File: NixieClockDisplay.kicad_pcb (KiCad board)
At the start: 2 copper layers, 160.1 x 160.1 mm, 59 parts, among them J1 CONN_01X08, J2 CONN_01X03, J3 CONN_01X03, U1 TPIC6B595, U2 TPIC6B595, U3 TPIC6B595, U4 TPIC6B595, U5 TPIC6B595, U6 TPIC6B595, U7 WE-FDSM_DC/DC_5V

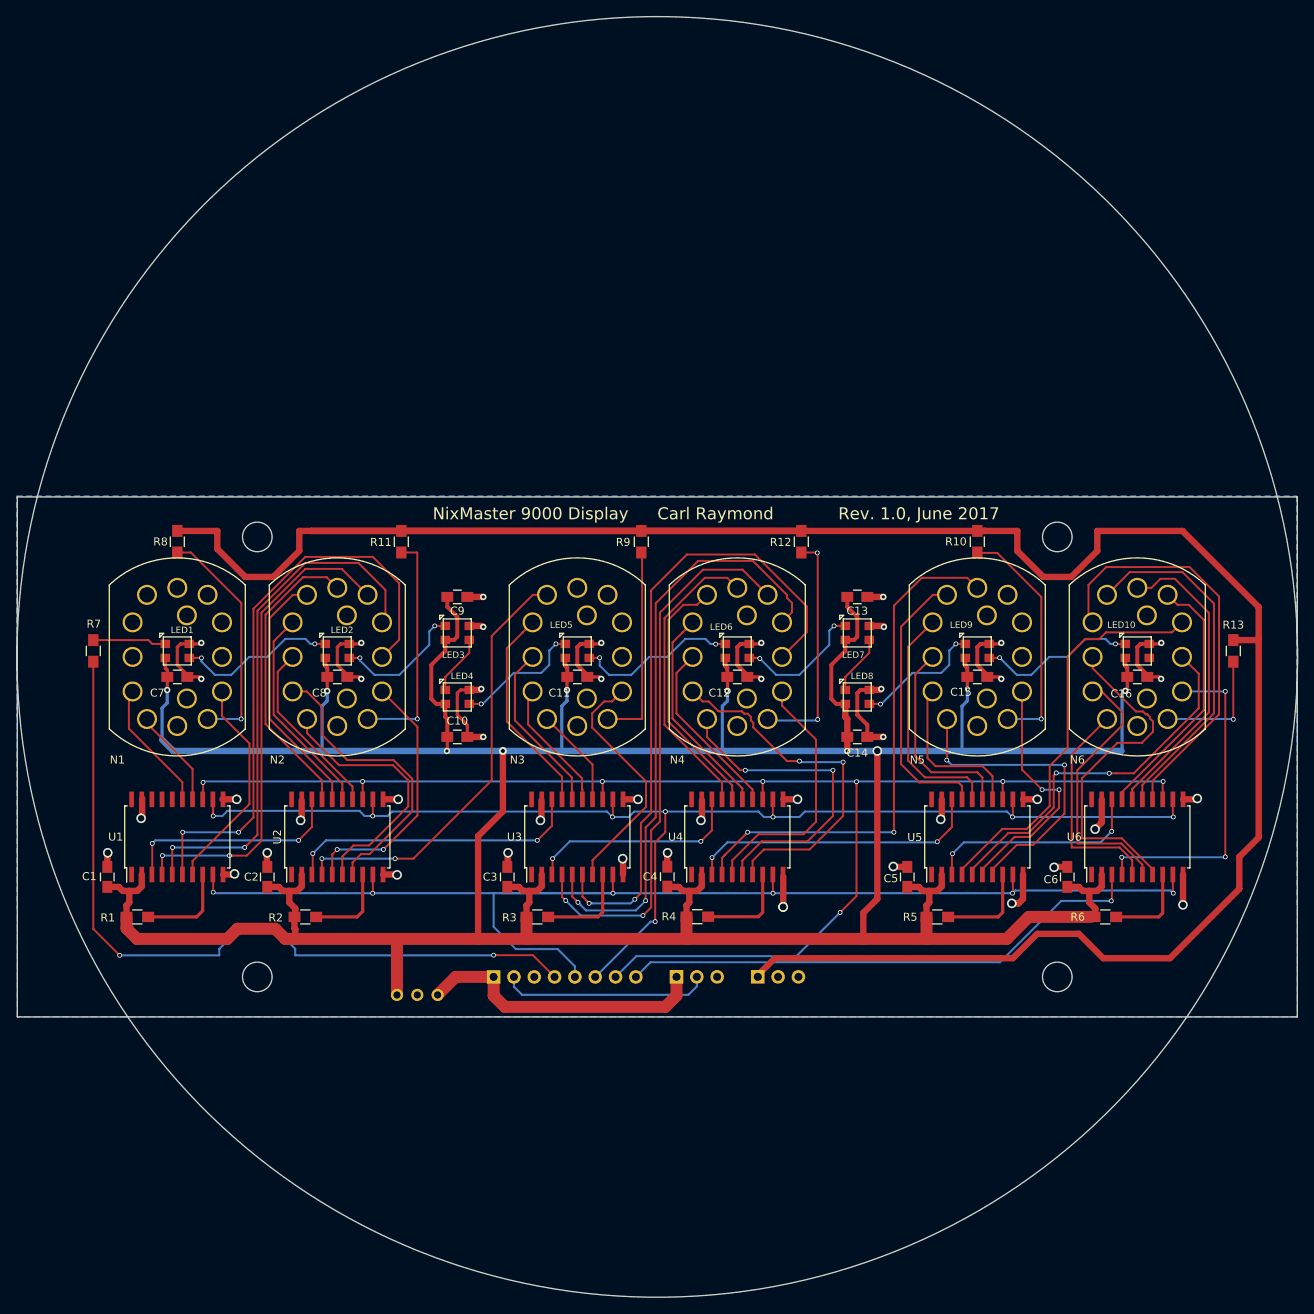
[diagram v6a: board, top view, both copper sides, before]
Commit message: Curved board outline
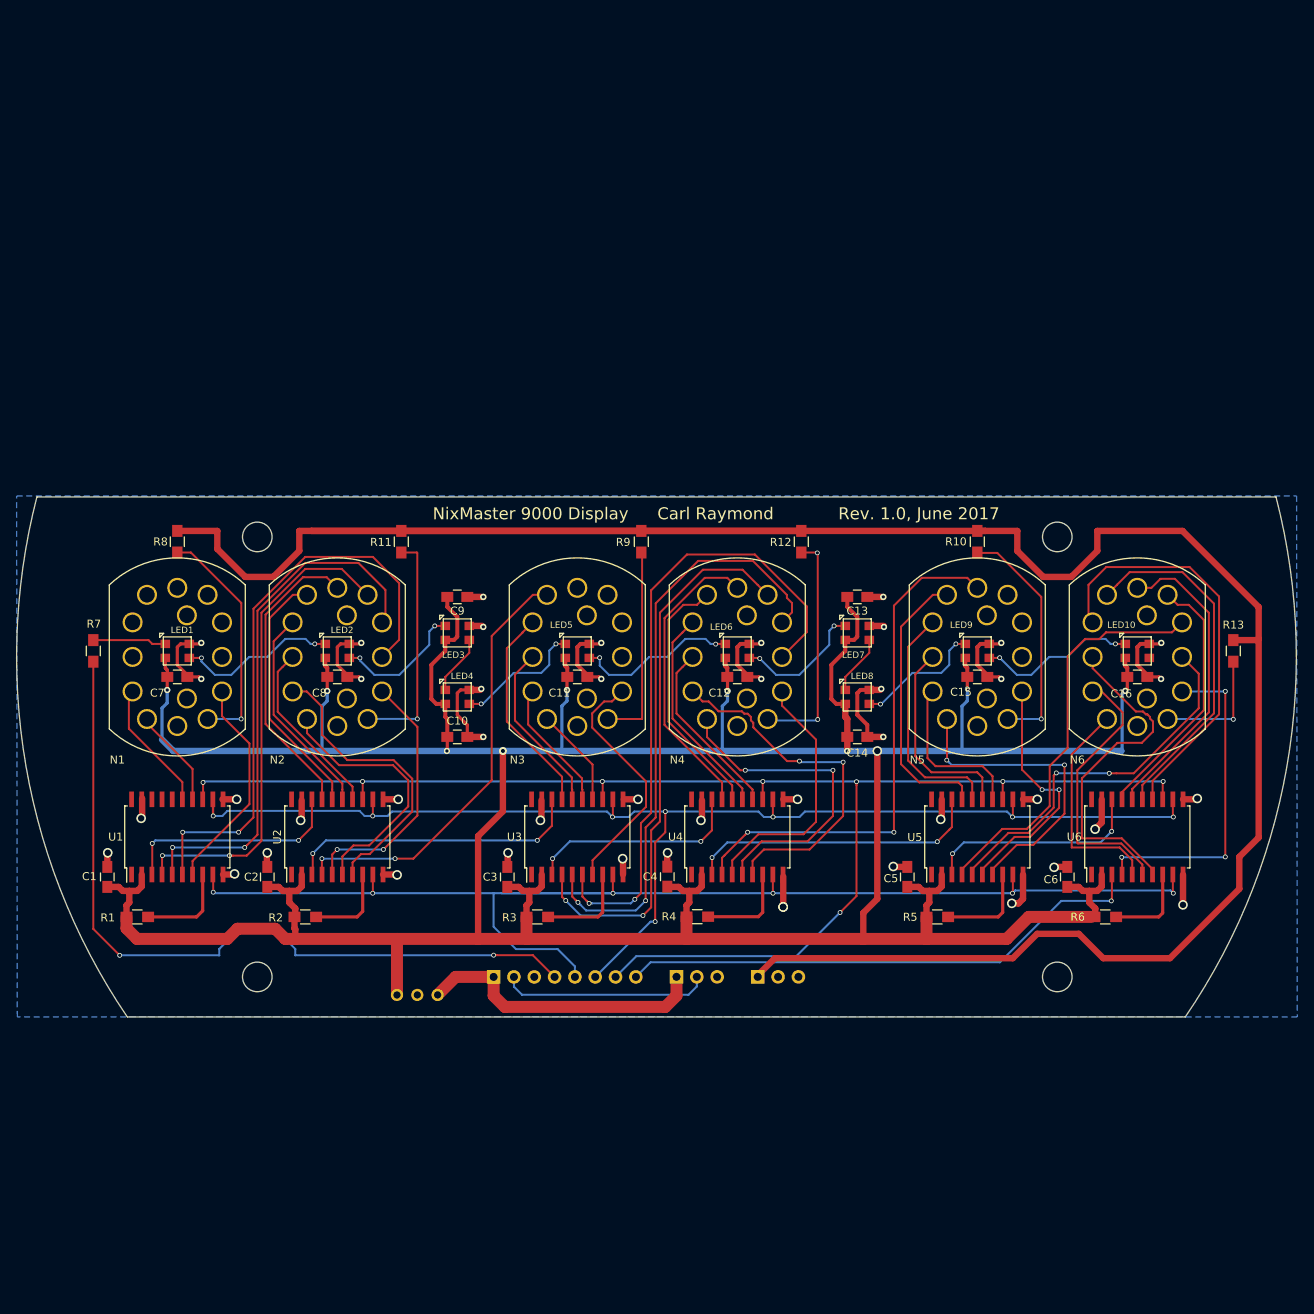
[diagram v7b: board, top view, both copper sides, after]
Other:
- board size 160.1 x 160.1 mm -> 160 x 65 mm
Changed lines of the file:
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@@
   (general
     (links 187)
-    (no_connects 3)
-    (area 69.885946 -20.114054 230.114054 140.350392)
+    (no_connects 0)
+    (area 69.837157 39.906641 229.956163 105.075001)
     (thickness 1.6)
-    (drawings 23)
+    (drawings 22)
     (tracks 1161)
     (zones 0)
@@
   )
   (setup
-    (last_trace_width 0.8)
+    (last_trace_width 0.25)
     (user_trace_width 0.4)
     (user_trace_width 0.5)
@@
     (pad 1 np_thru_hole circle (at 0 0) (size 3.7 3.7) (drill 3.7) (layers *.Cu *.Mask))
   )
-  (gr_circle (center 150 60) (end 230 57.5) (layer Edge.Cuts) (width 0.15))
+  (gr_arc (start 150 60) (end 83.75 105) (angle 48.65) (layer Edge.Cuts) (width 0.15))
+  (gr_arc (start 150 60) (end 216 105) (angle -48.785) (layer Edge.Cuts) (width 0.15))
+  (gr_line (start 216 105) (end 83.75 105) (layer Edge.Cuts) (width 0.15))
+  (gr_line (start 72.45 40) (end 227.33 40) (layer Edge.Cuts) (width 0.15))
   (gr_text "Rev. 1.0, June 2017\n" (at 182.7 42.1) (layer F.SilkS)
     (effects (font (size 1.5 1.5) (thickness 0.3)))
@@
   (gr_circle (center 150 60.25) (end 70 60) (layer Dwgs.User) (width 0.2))
   (gr_circle (center 150 60) (end 78 60) (layer Dwgs.User) (width 0.2))
-  (gr_line (start 70 105) (end 70 40) (layer Edge.Cuts) (width 0.15))
-  (gr_line (start 230 105) (end 70 105) (layer Edge.Cuts) (width 0.15))
-  (gr_line (start 230 40) (end 230 105) (layer Edge.Cuts) (width 0.15))
-  (gr_line (start 70 40) (end 230 40) (layer Edge.Cuts) (width 0.15))
   (segment (start 195.158528 90.805) (end 194.31 90.805) (width 0.8) (layer F.Cu) (net 1))
   (segment (start 195.715 90.248528) (end 195.158528 90.805) (width 0.8) (layer F.Cu) (net 1))

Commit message: Finalized board
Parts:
- added J4: CONN_02X04, Pin_Headers:Pin_Header_Straight_2x04_Pitch2.54mm, B.Cu at (77.2, 57.5)
- added J5: CONN_01X02, Pin_Headers:Pin_Header_Straight_1x02_Pitch2.54mm, B.Cu at (225.0, 60.0)
- moved R7 5.81 mm to (77.0, 54.0), turned to 180 degrees
- moved R13 4.25 mm to (222.0, 55.0)
- moved U7 4.20 mm to (115.8, 100.1)
- renumbered R9 to R10, R12 to R11, R10 to R12, R11 to R9
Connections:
- R7 pad 2: /PIXEL_IN -> Net-(J4-Pad2)
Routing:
- net +5V: track 488.9 -> 532.5 mm
- net GND: track 141.5 -> 155.5 mm, vias 45 -> 47
- net /PIXEL_IN: track 97.0 -> 101.9 mm, vias 2 -> 1
- net Net-(LED1-Pad3): track 9.20 -> 13.3 mm
- net Net-(J4-Pad2): track 0.00 -> 3.91 mm
- net /SEC_0: track 41.2 -> 38.0 mm
- net +12V: track 36.7 -> 39.9 mm
- net Net-(N6-Pad1): track 15.4 -> 18.3 mm
- net /RING_OUT: track 0.00 -> 2.54 mm
- net /RING_IN: track 0.00 -> 2.54 mm
- net /RCK: track 162.0 -> 160.4 mm
- net /HV: track 323.5 -> 325.0 mm
- net /MIN_9: track 81.0 -> 81.7 mm
- net /SEC_20: track 20.6 -> 20.0 mm
- net Net-(N4-Pad1): vias 2 -> 1
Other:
- board text added: "+5V"
- board text added: "1"
- board text added: "2"
- board text added: "3"
- board text added: "4"
- board text added: "DIN"
- board text added: "DOUT"
- board text added: "NIXIE DIN"
- board text added: "PIXEL DIN"
- board text added: "Shunt 1-2 to omit ring Shunt 1-3 and 2-4 for ring DOUT to ring DIN Ring DOUT to DIN"
- board text removed: "DATA IN"
- board text removed: "PIXEL IN"
